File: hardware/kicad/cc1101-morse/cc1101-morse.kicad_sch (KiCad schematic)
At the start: 7 parts, among them J1 Conn_02x04_Odd_Even, SW1 SW_Push, U1 ESP32-C3-SuperMini

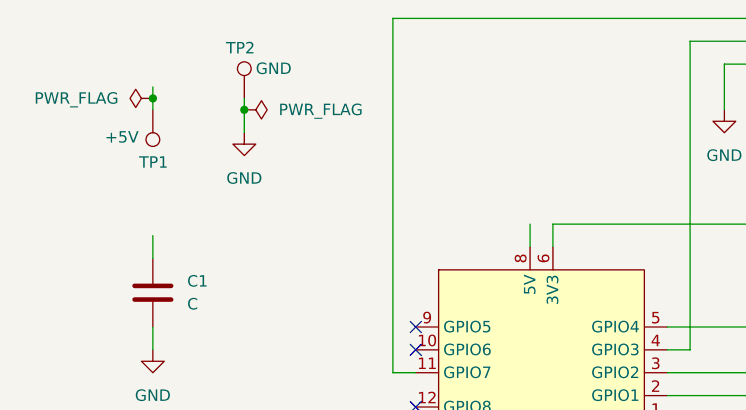
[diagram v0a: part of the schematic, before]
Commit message: Correct schematic status: ERC clean, netlist verified
The previous commit claimed the schematic shorted every net into one
32-node net across the supply. That was wrong — a bad regex in the
netlist check concatenated all 15 nets into one blob, and the empty
power-symbol pin names offered as corroboration are normal in KiCad
10 (the stock power library has them too).

The schematic was correct all along. Verified: 15 nets, every
connection matching the pin table — SPI on GPIO2/3/4, CSN GPIO1,
GDO0 GPIO0, GDO2 GPIO7, key GPIO10, buzzer GPIO20, GPIO5/6/8/9/21
unconnected.

Remaining: C1 has no footprint, and J1 wants renaming to J2 since
the BOM reserves J1 for the antenna.
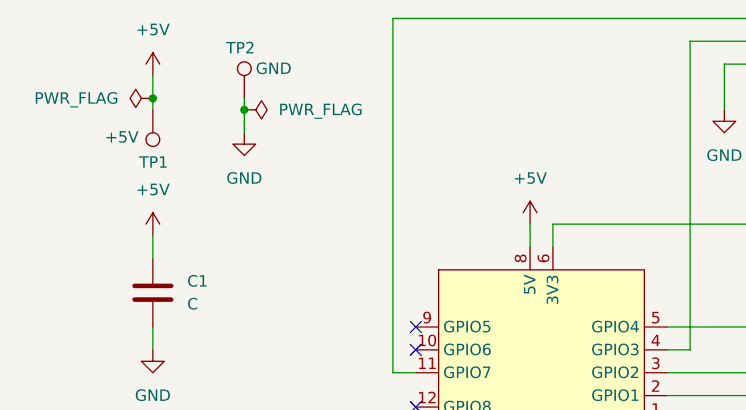
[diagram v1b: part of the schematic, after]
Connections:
- net +5V: now reaches TP1.1
- net +5V: now also C1.1, U1.8 (5V)
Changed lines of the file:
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@@
-	(wire
-		(pts
-			(xy 113.03 64.77) (xy 113.03 63.5)
-		)
-		(stroke
-			(width 0)
-			(type default)
-		)
-	)
 	(wire
 		(pts
 			(xy 189.23 60.96) (xy 189.23 63.5)
+		)
+		(stroke
+			(width 0)
+			(type default)
+		)
+	)
+	(wire
+		(pts
+			(xy 113.03 62.23) (xy 113.03 64.77)
 		)
 		(stroke
@@
 	)
 	(symbol
+		(lib_id "power:+5V")
+		(at 113.03 80.01 0)
+		(unit 1)
+		(body_style 1)
+		(exclude_from_sim no)
+		(in_bom yes)
+		(on_board yes)
+		(in_pos_files yes)
+		(dnp no)
+		(fields_autoplaced yes)
+		(property "Reference" "#PWR09"
+			(at 113.03 83.82 0)
+			(hide yes)
+			(show_name no)
+			(do_not_autoplace no)
+			(effects
+				(font
+					(size 1.27 1.27)
+				)
+			)
+		)
+		(property "Value" "+5V"
+			(at 113.03 74.93 0)
+			(show_name no)
+			(do_not_autoplace no)
+			(effects
+				(font
+					(size 1.27 1.27)
+				)
+			)
+		)
+		(property "Footprint" ""
+			(at 113.03 80.01 0)
+			(hide yes)
+			(show_name no)
+			(do_not_autoplace no)
+			(effects
+				(font
+					(size 1.27 1.27)
+				)
+			)
+		)
+		(property "Datasheet" ""
+			(at 113.03 80.01 0)
+			(hide yes)
+			(show_name no)
+			(do_not_autoplace no)
+			(effects
+				(font
+					(size 1.27 1.27)
+				)
+			)
+		)
+		(property "Description" "Power symbol creates a global label with name \"+5V\""
+			(at 113.03 80.01 0)
+			(hide yes)
+			(show_name no)
+			(do_not_autoplace no)
+			(effects
+				(font
+					(size 1.27 1.27)
+				)
+			)
+		)
+		(pin "1"
+		)
+		(instances
+			(project "cc1101-morse"
+				(path "/a13f60b2-a387-4aea-a9eb-c0b400a12521"
+					(reference "#PWR09")
+					(unit 1)
+				)
+			)
+		)
+	)
+	(symbol
+		(lib_id "power:+5V")
+		(at 113.03 62.23 0)
+		(unit 1)
+		(body_style 1)
+		(exclude_from_sim no)
+		(in_bom yes)
+		(on_board yes)
+		(in_pos_files yes)
+		(dnp no)
+		(fields_autoplaced yes)
+		(property "Reference" "#PWR08"
+			(at 113.03 66.04 0)
+			(hide yes)
+			(show_name no)
+			(do_not_autoplace no)
+			(effects
+				(font
+					(size 1.27 1.27)
+				)
+			)
+		)
+		(property "Value" "+5V"
+			(at 113.03 57.15 0)
+			(show_name no)
+			(do_not_autoplace no)
+			(effects
+				(font
+					(size 1.27 1.27)
+				)
+			)
+		)
+		(property "Footprint" ""
+			(at 113.03 62.23 0)
+			(hide yes)
+			(show_name no)
+			(do_not_autoplace no)
+			(effects
+				(font
+					(size 1.27 1.27)
+				)
+			)
+		)
+		(property "Datasheet" ""
+			(at 113.03 62.23 0)
+			(hide yes)
+			(show_name no)
+			(do_not_autoplace no)
+			(effects
+				(font
+					(size 1.27 1.27)
+				)
+			)
+		)
+		(property "Description" "Power symbol creates a global label with name \"+5V\""
+			(at 113.03 62.23 0)
+			(hide yes)
+			(show_name no)
+			(do_not_autoplace no)
+			(effects
+				(font
+					(size 1.27 1.27)
+				)
+			)
+		)
+		(pin "1"
+		)
+		(instances
+			(project "cc1101-morse"
+				(path "/a13f60b2-a387-4aea-a9eb-c0b400a12521"
+					(reference "#PWR08")
+					(unit 1)
+				)
+			)
+		)
+	)
+	(symbol
 		(lib_id "Connector_Generic:Conn_02x04_Odd_Even")
 		(at 184.15 71.12 90)
@@
 					(unit 1)
 				)
+			)
+		)
+	)
+	(symbol
+		(lib_id "power:+5V")
+		(at 154.94 78.74 0)
+		(unit 1)
+		(body_style 1)
+		(exclude_from_sim no)
+		(in_bom yes)
+		(on_board yes)
+		(in_pos_files yes)
+		(dnp no)
+		(fields_autoplaced yes)
+		(property "Reference" "#PWR07"
+			(at 154.94 82.55 0)
+			(hide yes)
+			(show_name no)
+			(do_not_autoplace no)
+			(effects
+				(font
+					(size 1.27 1.27)
+				)
+			)
+		)
+		(property "Value" "+5V"
+			(at 154.94 73.66 0)
+			(show_name no)
+			(do_not_autoplace no)
+			(effects
+				(font
+					(size 1.27 1.27)
+				)
+			)
+		)
+		(property "Footprint" ""
+			(at 154.94 78.74 0)
+			(hide yes)
+			(show_name no)
+			(do_not_autoplace no)
+			(effects
+				(font
+					(size 1.27 1.27)
+				)
+			)
+		)
+		(property "Datasheet" ""
+			(at 154.94 78.74 0)
+			(hide yes)
+			(show_name no)
+			(do_not_autoplace no)
+			(effects
+				(font
+					(size 1.27 1.27)
+				)
+			)
+		)
+		(property "Description" "Power symbol creates a global label with name \"+5V\""
+			(at 154.94 78.74 0)
+			(hide yes)
+			(show_name no)
+			(do_not_autoplace no)
+			(effects
+				(font
+					(size 1.27 1.27)
+				)
+			)
+		)
+		(pin "1"
+		)
+		(instances
+			(project "cc1101-morse"
+				(path "/a13f60b2-a387-4aea-a9eb-c0b400a12521"
+					(reference "#PWR07")
+					(unit 1)
+				)

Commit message: Correct CC1101 socket pin order to match Sparks
The pin table assumed VCC on pin 1 and MOSI/SCK on 3/4. The real
module — and Sparks, which wires one — has GND on pin 1, VCC on 2,
and SCK before MOSI on 5/6. The supply pair was inverted, which is
the mistake that destroys the module.

Correct order, from the 433M silkscreen:
  1 GND   2 VCC   3 GDO0   4 CSN   5 SCK   6 MOSI   7 MISO   8 GDO2

Firmware is unaffected: the GPIO-to-function assignments are
unchanged, only which socket pin each one lands on.

Also fixes the buzzer footprint name, which had a trailing "mm" the
KiCad library does not use (Buzzer_12x9.5RM7.6, not ...RM7.6mm).
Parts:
- BZ1: footprint (none) -> Buzzer_Beeper:Buzzer_12x9.5RM7.6
- C1: footprint (none) -> Capacitor_THT:C_Disc_D5.0mm_W2.5mm_P5.00mm
- J1: footprint Connector_PinHeader_2.54mm:PinHeader_2x04_P2.54mm_Vertical -> Connector_PinSocket_2.54mm:PinSocket_2x04_P2.54mm_Vertical
- SW1: footprint (none) -> Button_Switch_THT:SW_PUSH_6mm
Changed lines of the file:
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@@
 			)
 		)
-		(property "Footprint" "Connector_PinHeader_2.54mm:PinHeader_2x04_P2.54mm_Vertical"
+		(property "Footprint" "Connector_PinSocket_2.54mm:PinSocket_2x04_P2.54mm_Vertical"
 			(at 184.15 71.12 0)
 			(hide yes)
@@
 			)
 		)
-		(property "Footprint" ""
+		(property "Footprint" "Button_Switch_THT:SW_PUSH_6mm"
 			(at 130.81 100.33 0)
 			(hide yes)
@@
 			)
 		)
-		(property "Footprint" ""
+		(property "Footprint" "Capacitor_THT:C_Disc_D5.0mm_W2.5mm_P5.00mm"
 			(at 113.9952 90.17 0)
 			(hide yes)
@@
 			)
 		)
-		(property "Footprint" ""
+		(property "Footprint" "Buzzer_Beeper:Buzzer_12x9.5RM7.6"
 			(at 132.715 113.03 90)
 			(hide yes)

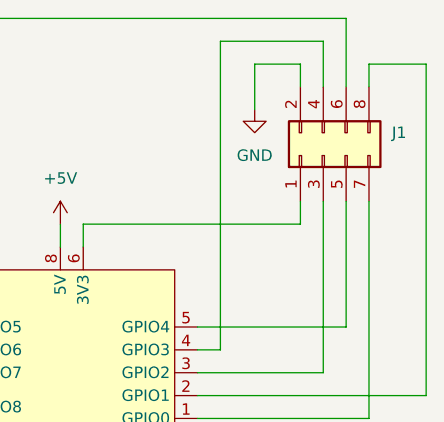
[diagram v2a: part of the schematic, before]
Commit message: Record design rules: 0.4 mm tracks, no net classes
No net classes — nothing on this board needs different physical rules
from anything else. Eight digital signals at Morse speeds plus power
and ground; nothing fast, high-current, or impedance-controlled.

0.4 mm sits wider than a fab house's 0.25 mm default, which is the
right direction for laser etching: the cut widens as it bites, so the
surviving copper is narrower than drawn.

Notes the one case worth revisiting — ground is a perimeter trace
rather than a pour, so it is a long thin strip taking every return
current and all the handling stress. Widening it is mechanical
insurance, not electrical.
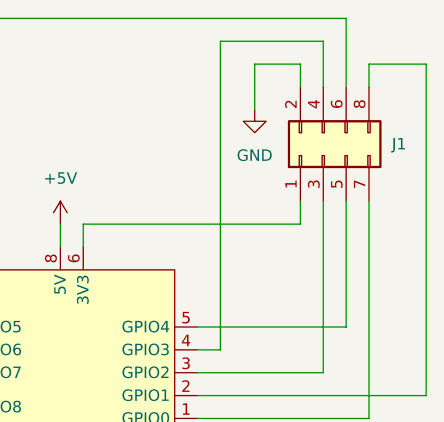
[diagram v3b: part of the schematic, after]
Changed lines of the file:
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@@
 		(fields_autoplaced yes)
 		(property "Reference" "J1"
-			(at 191.77 68.5799 90)
+			(at 191.77 69.8499 90)
 			(show_name no)
 			(do_not_autoplace no)

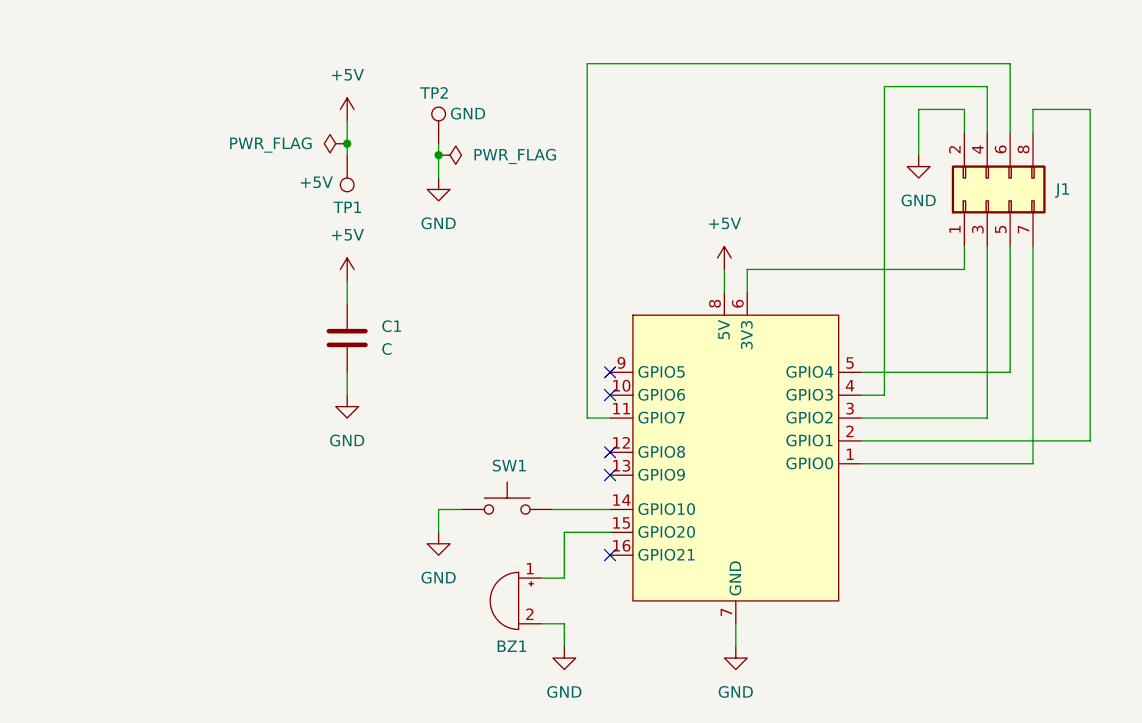
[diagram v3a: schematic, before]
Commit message: Board: GND pour, mounting holes, J1 rewired to new pins
The schematic now matches the reassigned SPI pins (MOSI GPIO6, SCK
GPIO5, MISO GPIO2) — verified against the netlist, all eight J1 pins
correct.

Ground is a filled zone on F.Cu rather than the perimeter trace
decisions.md §3 specified. The pour is the better choice here and the
earlier objection to it was wrong: the board is 40x60 mm with 17
thin traces, so there is no fragmentation risk, and the connection
the autorouter could not make (BZ1.2 -> J1.2) is solved for free by
both pads dropping into the fill. It also suits the process — a fiber
laser removes copper, so leaving a pour is less etching, not more.

Four mounting holes added, one per corner, inset ~3 mm.
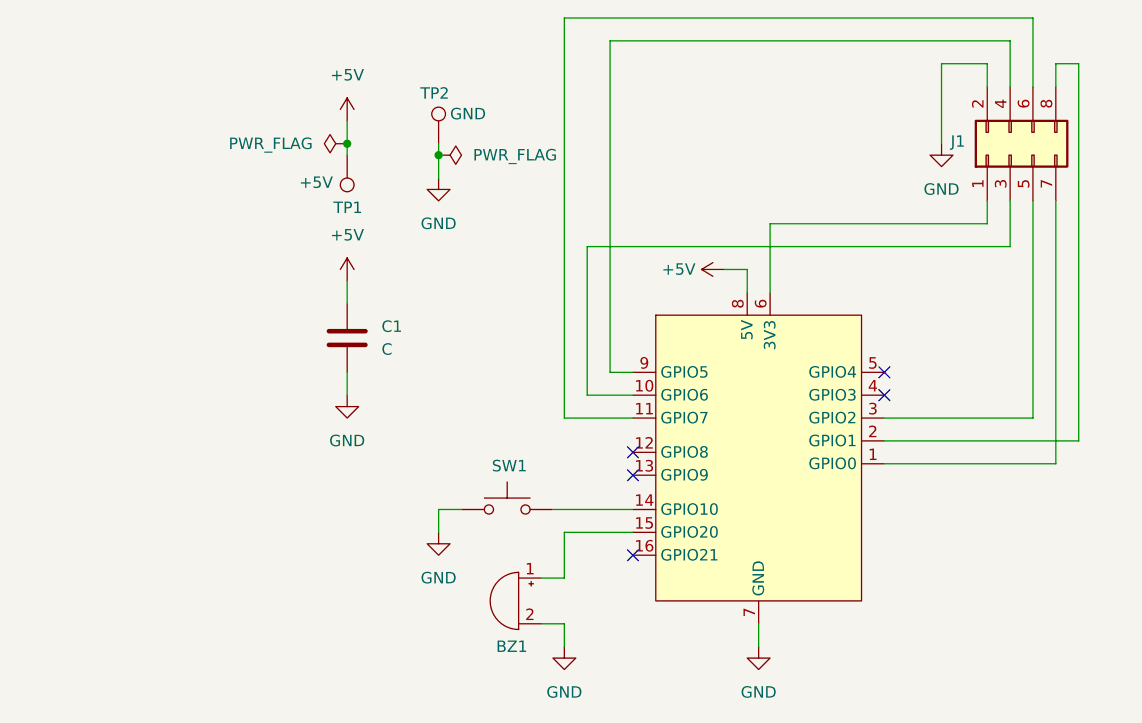
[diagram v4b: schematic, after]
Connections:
- net at J1.3 (Pin_3): now also U1.10 (GPIO6); no longer U1.3 (GPIO2)
- net at J1.4 (Pin_4): now also U1.9 (GPIO5); no longer U1.4 (GPIO3)
- net at J1.5 (Pin_5): now also U1.3 (GPIO2); no longer U1.5 (GPIO4)
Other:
- moved on the sheet: J1

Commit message: Add C2, decoupling the CC1101's own 3V3 rail
C1 sits across +5V near the Supermini — input decoupling for the
regulator, which is a real job but not the radio's. The CC1101 runs
from +3V3 and had no local capacitor at all.

C2 fills that gap. In TX the radio switches ~35 mA on and off at
keying speed while SPI is bit-banged alongside it, so every mark is a
step change in current. The regulator answers in microseconds and the
trace to the socket has inductance; C2 supplies that first instant
locally.

Likely unnecessary at these currents, but the failure mode if it is
needed and missing — intermittent SPI errors, or the radio dropping
out only while transmitting — is much worse to diagnose than one
through-hole part is to fit.

Docs corrected throughout: the BOM described C1 as "CC1101 supply
decoupling, place close to the socket's VCC pin", which was the job
C2 now does.

DRC clean: 0 violations, 0 unconnected, 0 parity.
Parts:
- added C2: 100n, Capacitor_THT:C_Disc_D5.0mm_W2.5mm_P5.00mm, symbol Device:C
- C1: value C -> 100n
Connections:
- net GND: now also C2.2
- net +3V3: now reaches J1.1 (Pin_1), U1.6 (3V3)
- net +3V3: now also C2.1
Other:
- moved on the sheet: C1, TP1

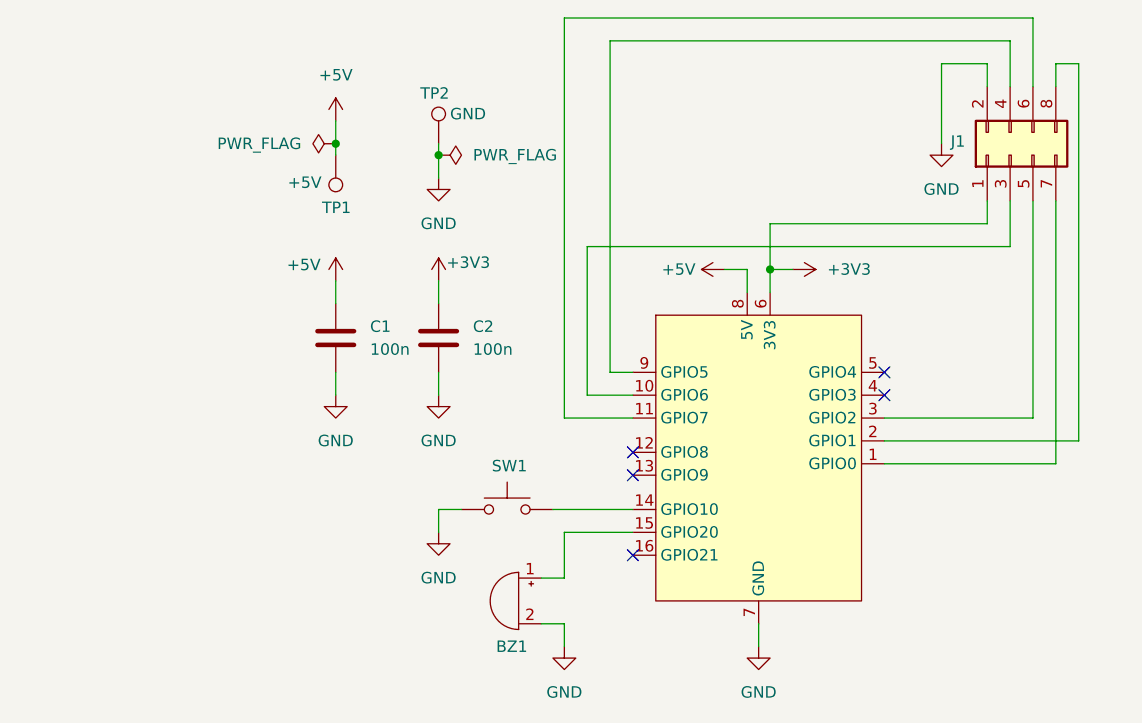
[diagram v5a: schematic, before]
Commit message: Fix the CC1101 socket pinout to match the module
J1 now carries the module's own order: GND, VCC, GDO0, CSN, SCK,
MOSI, MISO, GDO2.

Two things were wrong before. The supply pair was reversed — pad 1
was +3V3 where the module has GND — so plugging a module into the
board would have applied power backwards across it. And all six
signals were offset, so nothing would have talked even had the module
survived.

Caught on the breadboard: status reported PARTNUM 0xFF VERSION 0xFF,
MISO stuck high, which is what a module that is not driving the bus
looks like.

The signals cost nothing to fix. Every SPI line here is bit-banged,
so no pin is special — radio.h just renames which GPIO is which
function, six #defines, no re-routing. Power was the exception: rails
are physical and that pair had to be corrected on the board.

DRC: 0 unconnected, 0 parity. The one remaining violation is a
footprint/library mismatch warning, expected after editing the
footprint's pad numbering.

Firmware compiles clean at 27% flash.
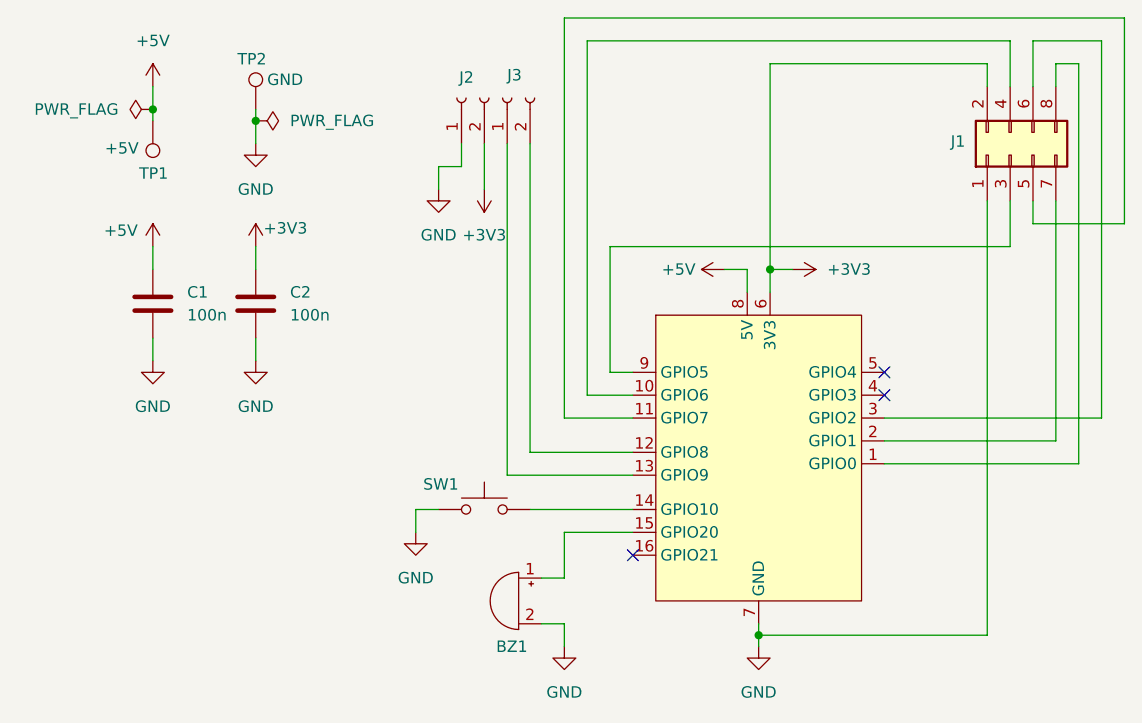
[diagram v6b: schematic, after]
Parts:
- added J2, J3: Conn_01x02_Socket, Connector_PinSocket_2.54mm:PinSocket_1x02_P2.54mm_Vertical, symbol Connector:Conn_01x02_Socket
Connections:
- net +3V3: now also J1.2 (Pin_2), J2.2 (Pin_2); no longer J1.1 (Pin_1)
- net GND: now also J1.1 (Pin_1), J2.1 (Pin_1); no longer J1.2 (Pin_2)
- net at J1.3 (Pin_3): now also U1.9 (GPIO5); no longer U1.10 (GPIO6)
- net at J1.4 (Pin_4): now also U1.10 (GPIO6); no longer U1.9 (GPIO5)
- net at J1.5 (Pin_5): now also U1.11 (GPIO7); no longer U1.3 (GPIO2)
- net at J1.6 (Pin_6): now also U1.3 (GPIO2); no longer U1.11 (GPIO7)
- net at J1.7 (Pin_7): now also U1.2 (GPIO1); no longer U1.1 (GPIO0)
- net at J1.8 (Pin_8): now also U1.1 (GPIO0); no longer U1.2 (GPIO1)
- net at U1.12 (GPIO8): now also J3.2 (Pin_2)
- net at U1.13 (GPIO9): now also J3.1 (Pin_1)
- no-connect marks 5 -> 3
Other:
- moved on the sheet: C1, C2, SW1, TP1, TP2

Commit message: Replace J2/J3 with one 4-pin display socket, plus a +3V3 wire link
J2 is now a single 1x4 female socket — GND, +3V3, GPIO9 (SCL),
GPIO8 (SDA) — so an SSD1306 plugs straight in instead of spanning two
separate 2-pin headers. J3 is gone.

+3V3 cannot reach it in copper. J1 pin 4 and its trace sit directly
between the rail and the connector, and on one layer a trace cannot
cross a trace. TP3 and TP4 are pads for a soldered wire link, which
§3 otherwise forbids, so §14 records why this one is allowed.

The workaround that looks better is worse. The rail can be threaded
between U1 pads 9 and 10 — 1.70 mm of gap against the 1.20 mm a
0.4 mm trace needs, and DRC passes. But it leaves ~0.25 mm of pour
either side, and that pour is the ground return for J1 pin 1, the
CC1101's ground. The trade is a visible wire against a severed RF
ground plane: one costs ten seconds of soldering, the other is
invisible, passes every check, and surfaces later as poor range.

DRC will report +3V3 unconnected. That is correct — the net arrives
in two pieces and the link is off-board. Two courtyard overlaps on
TP4/U1 are also expected: the ESP32 sits on female headers, so its
body clears a pad underneath.

Exports regenerated. 46 holes now, 11 parts to solder; counts updated
across the docs.
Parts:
- removed J2, J3: Conn_01x02_Socket, Connector_PinSocket_2.54mm:PinSocket_1x02_P2.54mm_Vertical, symbol Connector:Conn_01x02_Socket
- added J2: Conn_01x04_Socket, Connector_PinSocket_2.54mm:PinSocket_1x04_P2.54mm_Vertical, symbol Connector:Conn_01x04_Socket
- added TP3, TP4: TestPoint, TestPoint:TestPoint_THTPad_2.0x2.0mm_Drill1.0mm, symbol Connector:TestPoint
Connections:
- net +3V3: now also J2.2 (Pin_2), TP3.1, TP4.1
- net GND: now also J2.1 (Pin_1)
- net at U1.13 (GPIO9): now also J2.3 (Pin_3)
- net at U1.12 (GPIO8): now also J2.4 (Pin_4)
